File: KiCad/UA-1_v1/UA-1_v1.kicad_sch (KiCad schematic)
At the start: 44 parts, among them IC1 74LVC4245APW,112, J1 RF_base, J2 RF_base_gnd, J3 12V, J4 UART_FW, J5 RF_mine, J6 RF_mine_gnd, U1 MP-N, U2 AMS1117-3.3, U3 ESP32-WROOM-32E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

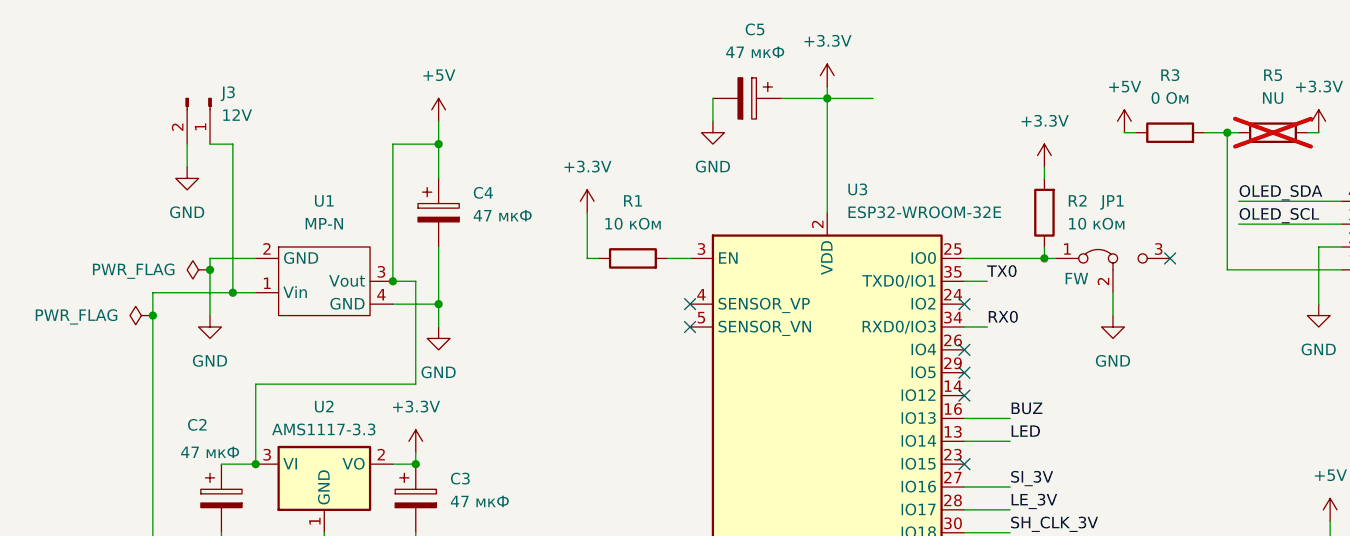
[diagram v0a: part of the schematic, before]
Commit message: add pls1-3
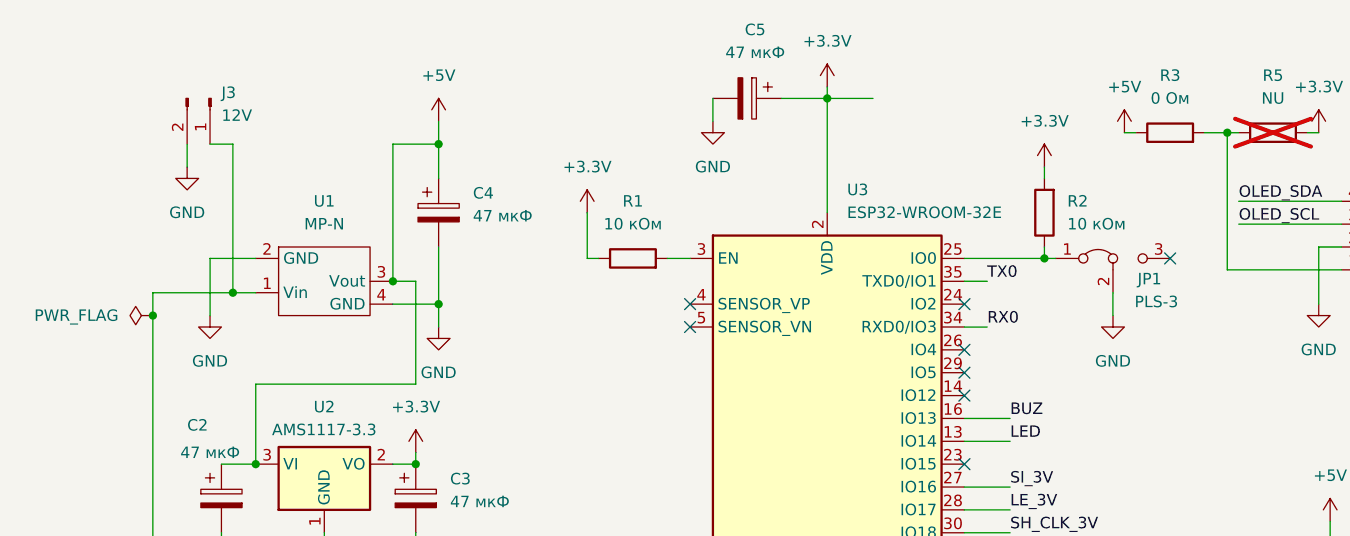
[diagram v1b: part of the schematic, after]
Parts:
- JP1: value FW -> PLS-3
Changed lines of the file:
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@@
 	)
 	(junction
-		(at 36.83 40.64)
-		(diameter 0)
-		(color 0 0 0 0)
-	)
-	(junction
 		(at 186.69 40.64)
 		(diameter 0)
@@
 	(wire
 		(pts
-			(xy 36.83 39.37) (xy 36.83 40.64)
+			(xy 36.83 39.37) (xy 36.83 45.72)
 		)
 		(stroke
@@
 	(wire
 		(pts
-			(xy 36.83 40.64) (xy 36.83 45.72)
-		)
-		(stroke
-			(width 0)
-			(type default)
-		)
-	)
-	(wire
-		(pts
 			(xy 260.35 128.27) (xy 260.35 130.81)
 		)
@@
 	)
 	(symbol
-		(lib_id "power:PWR_FLAG")
-		(at 36.83 40.64 90)
-		(unit 1)
-		(exclude_from_sim no)
-		(in_bom yes)
-		(on_board yes)
-		(dnp no)
-		(fields_autoplaced yes)
-		(property "Reference" "#FLG01"
-			(at 34.925 40.64 0)
-			(effects
-				(font
-					(size 1.27 1.27)
-				)
-				(hide yes)
-			)
-		)
-		(property "Value" "PWR_FLAG"
-			(at 33.02 40.6399 90)
-			(effects
-				(font
-					(size 1.27 1.27)
-				)
-				(justify left)
-			)
-		)
-		(property "Footprint" ""
-			(at 36.83 40.64 0)
-			(effects
-				(font
-					(size 1.27 1.27)
-				)
-				(hide yes)
-			)
-		)
-		(property "Datasheet" "~"
-			(at 36.83 40.64 0)
-			(effects
-				(font
-					(size 1.27 1.27)
-				)
-				(hide yes)
-			)
-		)
-		(property "Description" "Special symbol for telling ERC where power comes from"
-			(at 36.83 40.64 0)
-			(effects
-				(font
-					(size 1.27 1.27)
-				)
-				(hide yes)
-			)
-		)
-		(pin "1"
-		)
-		(instances
-			(project "UA-1_v1"
-				(path "/51c17e9b-7dab-4c11-afbb-666453ecee80"
-					(reference "#FLG01")
-					(unit 1)
-				)
-			)
-		)
-	)
-	(symbol
 		(lib_id "power:GND")
 		(at 248.92 44.45 0)
@@
 		(dnp no)
 		(property "Reference" "JP1"
-			(at 137.16 33.02 0)
+			(at 141.224 41.656 0)
 			(effects
 				(font
@@
 			)
 		)
-		(property "Value" "FW"
-			(at 133.096 41.656 0)
+		(property "Value" "PLS-3"
+			(at 141.986 44.196 0)
 			(effects
 				(font
